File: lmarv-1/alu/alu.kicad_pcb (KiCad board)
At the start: 4 copper layers, 158 x 115.2 mm, 120 parts, among them J1 Conn_02x03_Odd_Even, P1 dual-pcie-cardedge_split, U1 74LVC541, U10 74LVC541_a, U11 74LVC541_a, U12 74LVC541_a, U13 74LVC541_a, U14 74LVC541, U15 AT28BV64B-20JU, U16 74LVC541, U17 74LVC541, U18 74LVC541, U19 74LVC541, U2 74LVC04, U20 74LVC541, U21 74LVC541, U22 74LVC541, U23 74LVC541, U24 74LVC541_a, U25 74LVC541_a, U26 74LVC541, U27 74LVC541, U28 IS61LV256AL, U29 IS61LV256AL, U3 74LVC32, U30 IS61LV256AL, U31 IS61LV256AL, U32 IS61LV256AL, U33 IS61LV256AL, U34 IS61LV256AL, U35 AT28BV256B-20JU, U36 AT28BV64B-20JU, U37 74LVC541, U38 74LVC541_a, U39 IS61LV256AL, U4 74HC590, U40 74LVC541, U41 74LVC541, U42 74LVC541, U43 74LVC541, U44 74LVC541, U45 IS61LV256AL, U46 IS61LV256AL, U47 IS61LV256AL, U48 IS61LV256AL, U49 IS61LV256AL, U5 74HC590, U50 IS61LV256AL, U51 IS61LV256AL, U52 IS61LV256AL, U53 74LVC541, U54 74LVC541, U55 74LVC541, U56 74LVC541, U6 74LVC541_a, U7 74LVC541_a, U8 74LVC541_a, U9 74LVC541_a

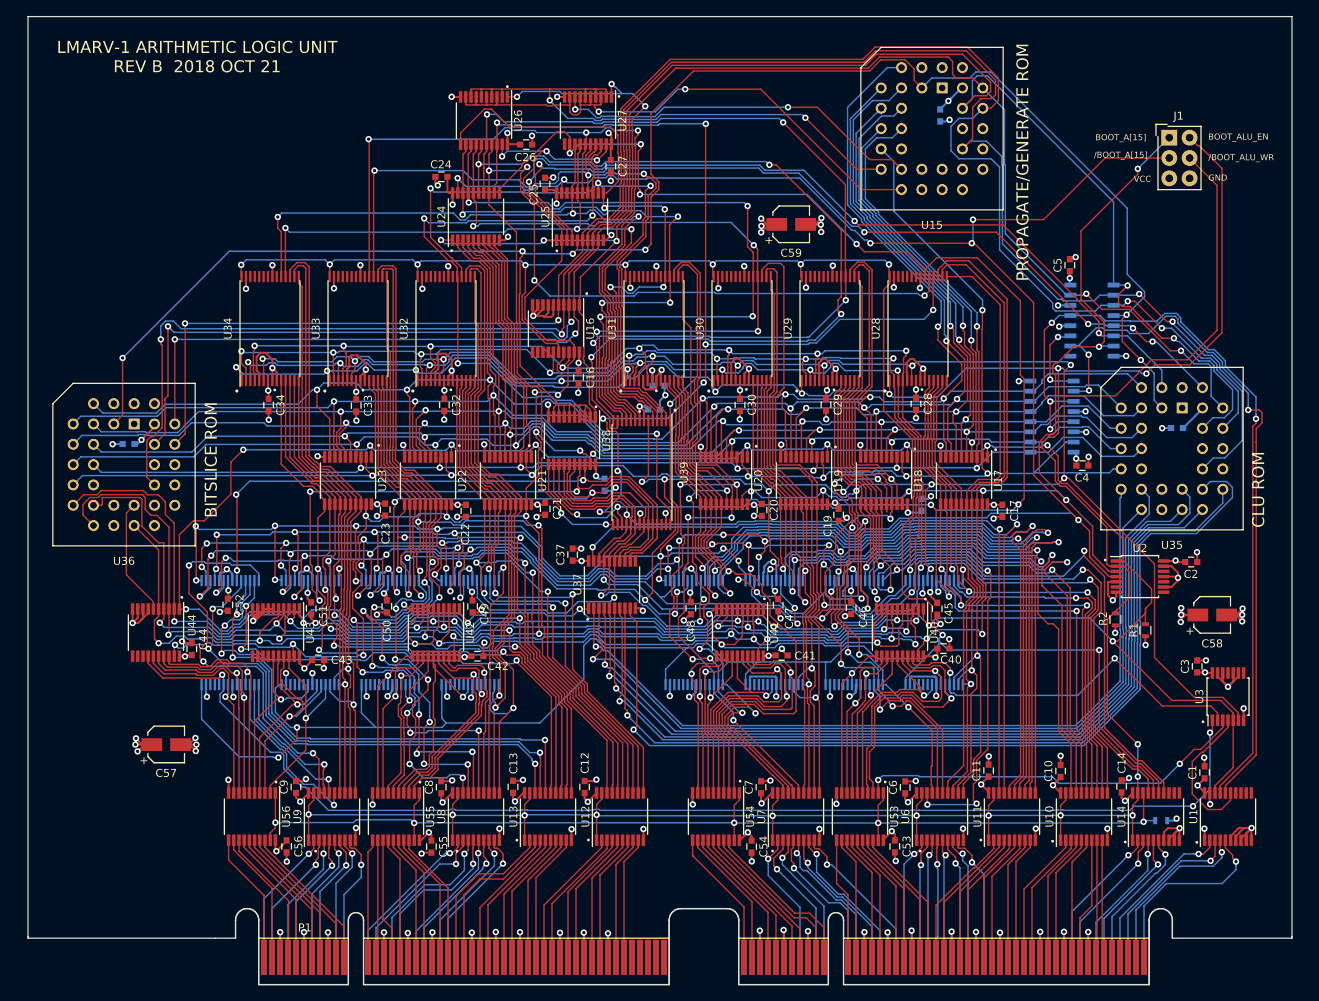
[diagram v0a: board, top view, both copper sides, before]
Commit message: ALU rev D, with simulations
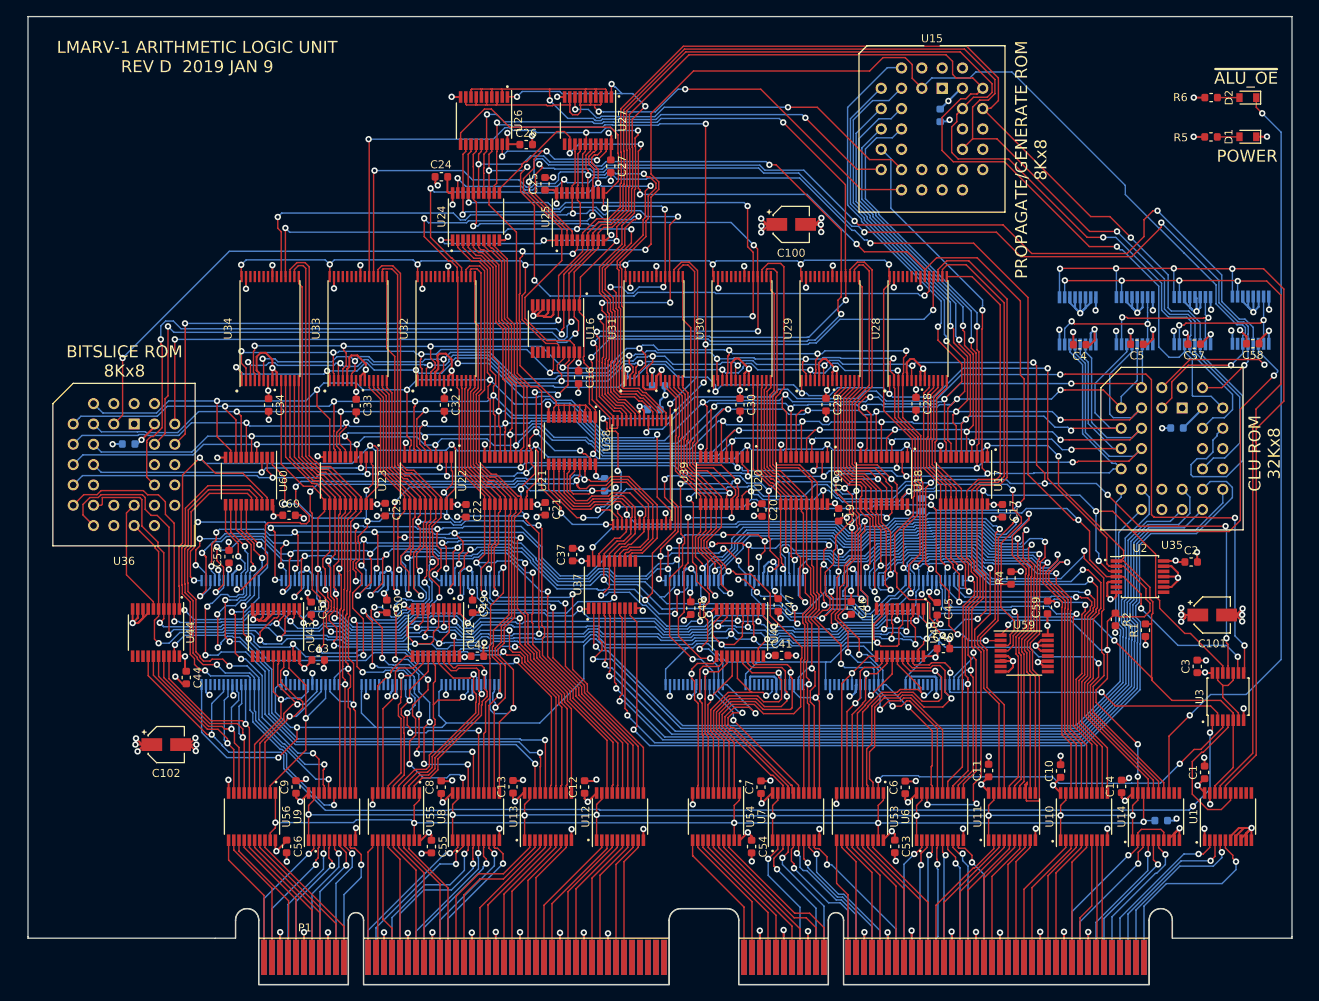
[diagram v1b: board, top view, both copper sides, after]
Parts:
- removed J1: Conn_02x03_Odd_Even, Connectors_Samtec:SDL-106-X-XX_2x03
- added C100: 1u, Capacitor_SMD:CP_Elec_4x4.5, F.Cu at (159.4, 56.0)
- added C101: 1u, Capacitor_SMD:CP_Elec_4x4.5, F.Cu at (212.0, 104.8)
- added C102: 1u, Capacitor_SMD:CP_Elec_4x4.5, F.Cu at (81.3, 121.0)
- added C60: 0u1, Capacitor_SMD:C_0603_1608Metric, F.Cu at (96.6, 92.3)
- added D1: APTD2012LSURCK, lmarv:D_0805_Wide, F.Cu at (216.5, 45.0)
- added D2: APTD2012LSURCK, lmarv:D_0805_Wide, F.Cu at (216.5, 40.1)
- added R4: 10k, Resistor_SMD:R_0603_1608Metric, F.Cu at (186.9, 100.2)
- added R5: 3k3, Resistor_SMD:R_0603_1608Metric, F.Cu at (211.9, 45.0)
- added R6: 3k3, Resistor_SMD:R_0603_1608Metric, F.Cu at (211.9, 40.1)
- added U57: 74LVC161, Package_SO:TSSOP-16_4.4x5mm_P0.65mm, B.Cu at (209.6, 68.0)
- added U58: 74LVC161, Package_SO:TSSOP-16_4.4x5mm_P0.65mm, B.Cu at (216.8, 67.9)
- added U59: 74LS157, Package_SO:TSSOP-16_4.4x5mm_P0.65mm, F.Cu at (188.5, 109.6)
- added U60: 74LVC541, Package_SO:TSSOP-20_4.4x6.5mm_P0.65mm, F.Cu at (91.6, 88.1)
- C1, C14, C15, C16, C2, C24, C25, C26, C27, C28, C29, C3, C30, C31, C32, C33, C34, C35, C36, C37, C38, C39, C4, C40, C41, C42, C43, C44, C45, C46, C47, C48, C49, C5, C50, C51, C52: footprint Capacitors_SMD:C_0603 -> Capacitor_SMD:C_0603_1608Metric
- C10, C11, C12, C13, C17, C18, C19, C20, C21, C22, C23, C53, C54, C55, C56, C6, C7, C8, C9: value 100n -> 0u1; footprint Capacitors_SMD:C_0603 -> Capacitor_SMD:C_0603_1608Metric
- C57, C58, C59: value 1u -> 100n; footprint Capacitors_SMD:CP_Elec_4x4.5 -> Capacitor_SMD:C_0603_1608Metric
- R1, R2, R3: footprint Resistors_SMD:R_0603 -> Resistor_SMD:R_0603_1608Metric
- U1, U14, U16, U17, U18, U19, U20, U21, U22, U23, U24, U25, U26, U27, U37, U38, U40, U41, U42, U43, U44: footprint Housings_SSOP:TSSOP-20_4.4x6.5mm_Pitch0.65mm -> Package_SO:TSSOP-20_4.4x6.5mm_P0.65mm
- U10, U11, U12, U13, U6, U7, U8, U9: value 74LVC541_a -> 74LVC541; footprint Housings_SSOP:TSSOP-20_4.4x6.5mm_Pitch0.65mm -> Package_SO:TSSOP-20_4.4x6.5mm_P0.65mm
- U15: footprint Sockets:PLCC32 -> Package_LCC:PLCC-32_THT-Socket
- U2, U3: footprint Housings_SSOP:TSSOP-14_4.4x5mm_Pitch0.65mm -> Package_SO:TSSOP-14_4.4x5mm_P0.65mm
- U4, U5: value 74HC590 -> 74LVC161; footprint Housings_SOIC:SOIC-16_3.9x9.9mm_Pitch1.27mm -> Package_SO:TSSOP-16_4.4x5mm_P0.65mm
- U53, U54, U55, U56: value 74LVC541 -> 74LVC541_a; footprint Housings_SSOP:TSSOP-20_4.4x6.5mm_Pitch0.65mm -> Package_SO:TSSOP-20_4.4x6.5mm_P0.65mm
- moved C57 137.9 mm to (209.8, 70.9), turned to 180 degrees
- moved C59 57.6 mm to (191.4, 103.8), turned to 90 degrees
- moved C58 34.3 mm to (217.1, 70.9), turned to 180 degrees
- moved C4 15.1 mm to (195.5, 71.0), turned to 180 degrees
- moved C5 13.0 mm to (202.6, 71.0), turned to 180 degrees
- moved U4 12.4 mm to (195.2, 68.0), turned to 270 degrees
- moved C52 6.02 mm to (89.1, 97.5), turned to 90 degrees
- moved U5 5.33 mm to (202.3, 68.0), turned to 270 degrees
- moved U15 5.19 mm to (178.3, 39.0)
- moved C44 3.64 mm to (83.8, 112.6), turned to 270 degrees
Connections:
- U14 pad 13: Net-(U14-Pad13) -> /~alu_oe_led
- U14 pad 7: GNDREF -> /~alu_oe'
- U21 pad 1: /~BOOT_ALU_EN -> /BOOT_A[15]
- U21 pad 19: /BOOT_A[15] -> /~BOOT_ALU_EN
- U22 pad 1: /~BOOT_ALU_EN -> /BOOT_A[15]
- U22 pad 19: /BOOT_A[15] -> /~BOOT_ALU_EN
- U23 pad 1: /~BOOT_ALU_EN -> /BOOT_A[15]
- U23 pad 19: /BOOT_A[15] -> /~BOOT_ALU_EN
- U28 pad 27: /~BOOT_ALU_WR -> /~BOOT_PH0_WR
- U29 pad 27: /~BOOT_ALU_WR -> /~BOOT_PH0_WR
- U3 pad 10: GNDREF -> /~BOOT_ALU_WR
- U3 pad 11: Net-(U3-Pad11) -> /~BOOT_PH0_WR
- U3 pad 12: GNDREF -> /BOOT_A[15]
- U3 pad 13: GNDREF -> /~BOOT_ALU_WR
- U3 pad 8: Net-(U3-Pad8) -> /~BOOT_PH1_WR
- U3 pad 9: GNDREF -> /~BOOT_A[15]
- U30 pad 27: /~BOOT_ALU_WR -> /~BOOT_PH0_WR
- U31 pad 27: /~BOOT_ALU_WR -> /~BOOT_PH0_WR
- U32 pad 27: /~BOOT_ALU_WR -> /~BOOT_PH0_WR
- U33 pad 27: /~BOOT_ALU_WR -> /~BOOT_PH0_WR
- U34 pad 27: /~BOOT_ALU_WR -> /~BOOT_PH0_WR
- U38 pad 11: /cin[0] -> /cin0_boot
- U39 pad 27: /~BOOT_ALU_WR -> /~BOOT_PH1_WR
- U4 pad 1: /BOOT_A[1] -> /~BOOT_RST
- U4 pad 10: /~BOOT_RST -> VCC
- U4 pad 11: /BOOT_CLK -> /BOOT_A[3]
- U4 pad 12: GNDREF -> /BOOT_A[2]
- U4 pad 13: /BOOT_CLK -> /BOOT_A[1]
- U4 pad 14: GNDREF -> /BOOT_A[0]
- U4 pad 15: /BOOT_A[0] -> /counter16/TC0
- U4 pad 2: /BOOT_A[2] -> /BOOT_CLK
- U4 pad 3: /BOOT_A[3] -> VCC
- U4 pad 4: /BOOT_A[4] -> VCC
- U4 pad 5: /BOOT_A[5] -> VCC
- U4 pad 6: /BOOT_A[6] -> VCC
- U4 pad 7: /BOOT_A[7] -> VCC
- U4 pad 9: /~BOOT_RCO -> VCC
- U45 pad 2: /cin[0] -> /cin0'
- U45 pad 27: /~BOOT_ALU_WR -> /~BOOT_PH0_WR
- U46 pad 27: /~BOOT_ALU_WR -> /~BOOT_PH0_WR
- U47 pad 27: /~BOOT_ALU_WR -> /~BOOT_PH0_WR
- U48 pad 27: /~BOOT_ALU_WR -> /~BOOT_PH0_WR
- U49 pad 27: /~BOOT_ALU_WR -> /~BOOT_PH0_WR
- U5 pad 1: /BOOT_A[9] -> /~BOOT_RST
- U5 pad 10: /~BOOT_RST -> /counter16/TC0
- U5 pad 11: /~BOOT_RCO -> /BOOT_A[7]
- U5 pad 12: GNDREF -> /BOOT_A[6]
- U5 pad 13: /BOOT_CLK -> /BOOT_A[5]
- U5 pad 14: GNDREF -> /BOOT_A[4]
- U5 pad 15: /BOOT_A[8] -> /counter16/TC1
- U5 pad 2: /BOOT_A[10] -> /BOOT_CLK
- U5 pad 3: /BOOT_A[11] -> VCC
- U5 pad 4: /BOOT_A[12] -> VCC
- U5 pad 5: /BOOT_A[13] -> VCC
- U5 pad 6: /BOOT_A[14] -> VCC
- U5 pad 7: /BOOT_A[15] -> /counter16/TC0
- U5 pad 9: Net-(U5-Pad9) -> VCC
- U50 pad 27: /~BOOT_ALU_WR -> /~BOOT_PH0_WR
- U51 pad 27: /~BOOT_ALU_WR -> /~BOOT_PH0_WR
- U52 pad 27: /~BOOT_ALU_WR -> /~BOOT_PH0_WR
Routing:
- net /~BOOT_ALU_WR: track 450.4 -> 9.87 mm, vias 28 -> 0
- net /~BOOT_PH0_WR: track 0.00 -> 394.7 mm, vias 0 -> 30
- net /~BOOT_PH1_WR: track 0.00 -> 117.4 mm, vias 0 -> 4
- net /~alu_oe_led: track 0.00 -> 96.6 mm, vias 0 -> 2
- net /cin0_boot: track 0.00 -> 91.7 mm, vias 0 -> 2
- net VCC: track 220.6 -> 289.2 mm, vias 74 -> 88
- net /rs1b[28]: track 21.8 -> 62.9 mm, vias 1 -> 2
- net /rs1b[29]: track 18.5 -> 57.8 mm, vias 1 -> 2
- net /BOOT_A[15]: track 391.7 -> 430.4 mm, vias 25 -> 29
- net /rs1b[30]: track 18.6 -> 56.7 mm, vias 1 -> 2
- net /~BOOT_ALU_EN: track 441.6 -> 476.0 mm
- net /BOOT_A[14]: track 105.1 -> 138.6 mm, vias 3 -> 4
- net /BOOT_ALU_EN: track 562.4 -> 532.9 mm, vias 35 -> 36
- net /counter16/TC1: track 0.00 -> 20.5 mm, vias 0 -> 2
- net /BOOT_A[1]: track 224.8 -> 244.9 mm, vias 8 -> 10
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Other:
- board text added: "BITSLICE ROM 8Kx8"
- board text added: "CLU ROM 32Kx8"
- board text added: "LMARV-1 ARITHMETIC LOGIC UNIT REV D 2019 JAN 9"
- board text added: "POWER"
- board text added: "PROPAGATE/GENERATE ROM 8Kx8"
- board text added: "~ALU_OE"
- board text removed: "/BOOT_ALU_WR"
- board text removed: "/BOOT_A[15]"
- board text removed: "BITSLICE ROM"
- board text removed: "BOOT_ALU_EN"
- board text removed: "BOOT_A[15]"
- board text removed: "CLU ROM"
- board text removed: "GND"
- board text removed: "LMARV-1 ARITHMETIC LOGIC UNIT REV B 2018 OCT 21"
- board text removed: "PROPAGATE/GENERATE ROM"
- board text removed: "VCC"
